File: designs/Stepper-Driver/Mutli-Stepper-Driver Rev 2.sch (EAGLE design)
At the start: 59 parts, among them IC1 PIC24FJ64GB002, J1 22-05-7048-04, J10 SON_OF_DARK_POWERSCH_22-05-70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, J11 SON_OF_DARK_POWERSCH_22-05-70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, J12 SON_OF_DARK_POWERSCH_22-05-70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, J2 22-05-7048-04, J3 22-05-7048-04, J4 22-05-7048-04, J5 22-05-7048-04, J6 22-05-7048-04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

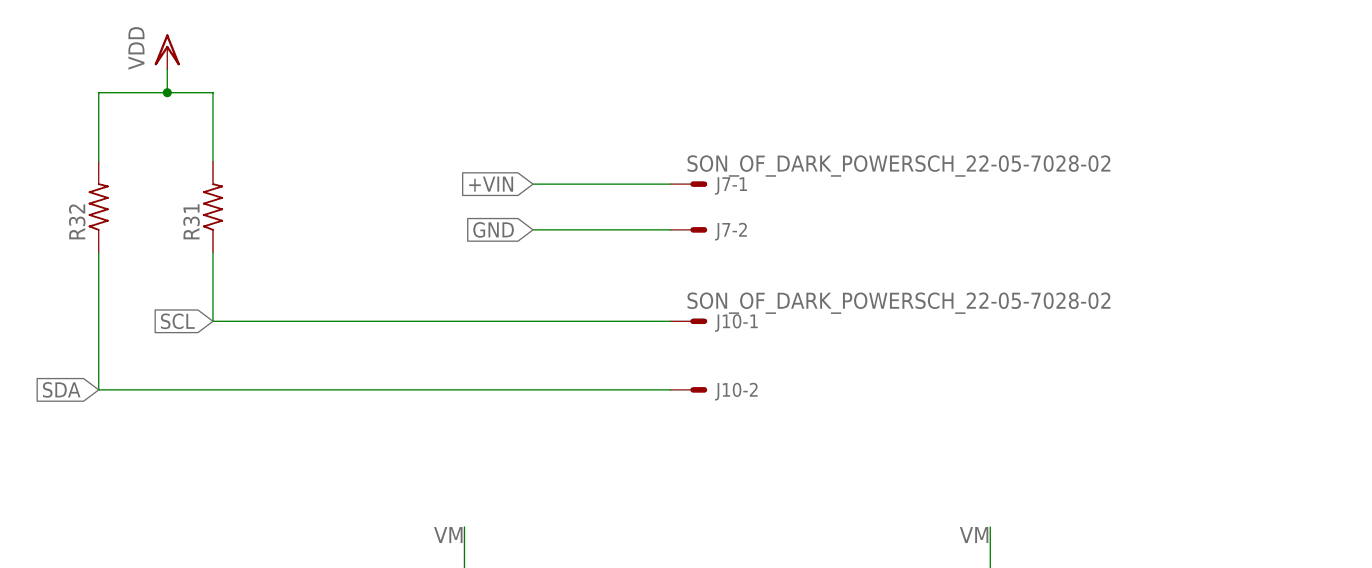
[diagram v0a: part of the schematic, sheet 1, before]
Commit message: removed extra part
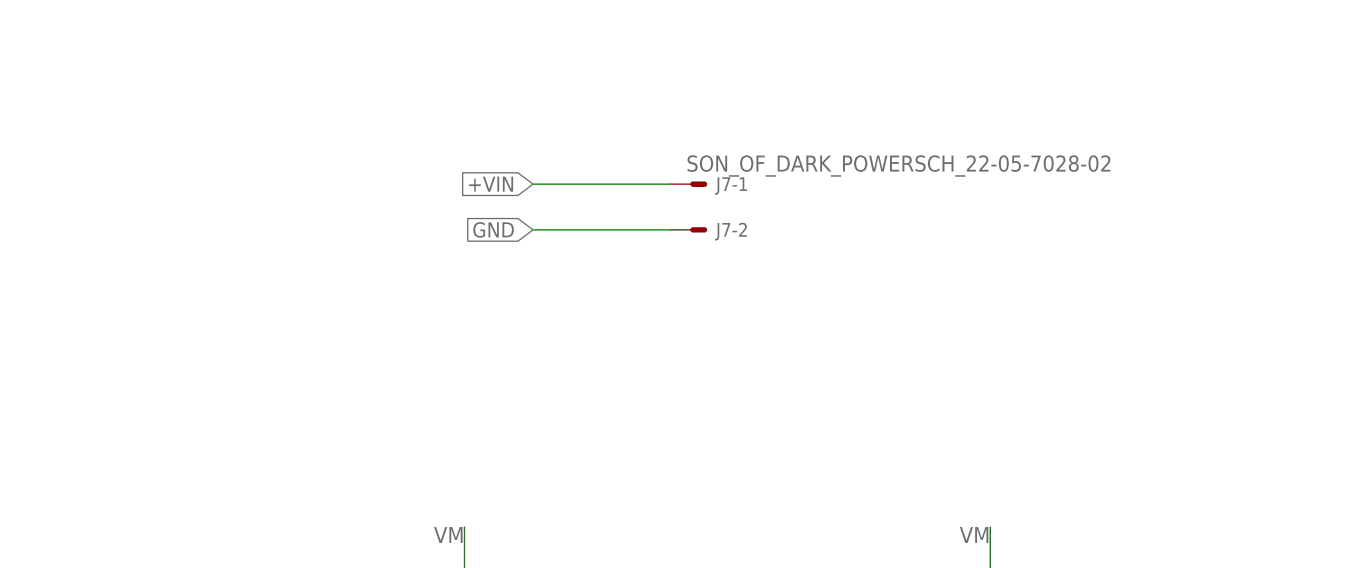
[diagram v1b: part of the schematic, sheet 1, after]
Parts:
- removed J10: SON_OF_DARK_POWERSCH_22-05-7028-02, MotherboardRev2:SON_OF_DARK_POWERSCH_22-05-7028-02
- removed R31, R32: (no value), rcl:R-US_R0805
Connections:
- removed net SCL: J10-1.S, R31.1
- removed net SDA: J10-2.S, R32.1
- net VDD: no longer R31.2, R32.2
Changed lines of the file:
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@@
 <part name="VDD6" library="supply1" deviceset="VDD" device=""/>
 <part name="GND29" library="supply1" deviceset="GND" device=""/>
-<part name="J10" library="MotherboardRev2" deviceset="SON_OF_DARK_POWERSCH_22-?-02" device="05-7028"/>
-<part name="R31" library="rcl" deviceset="R-US_" device="R0805"/>
-<part name="R32" library="rcl" deviceset="R-US_" device="R0805"/>
-<part name="VDD7" library="supply1" deviceset="VDD" device=""/>
 <part name="R33" library="rcl" deviceset="R-US_" device="R0805"/>
 <part name="LED1" library="led" deviceset="LED" device="CHIPLED_0805"/>
@@
 <instance part="VDD6" gate="G$1" x="119.38" y="76.2"/>
 <instance part="GND29" gate="1" x="129.54" y="22.86"/>
-<instance part="J10" gate="-1" x="81.28" y="218.44"/>
-<instance part="J10" gate="-2" x="81.28" y="210.82"/>
-<instance part="R31" gate="G$1" x="27.94" y="231.14" rot="R90"/>
-<instance part="R32" gate="G$1" x="15.24" y="231.14" rot="R90"/>
-<instance part="VDD7" gate="G$1" x="22.86" y="248.92"/>
 <instance part="R33" gate="G$1" x="170.18" y="157.48" rot="R90"/>
 <instance part="LED1" gate="G$1" x="170.18" y="147.32"/>
@@
 </segment>
 </net>
-<net name="SDA" class="0">
-<segment>
-<pinref part="J10" gate="-2" pin="S"/>
-<wire x1="78.74" y1="210.82" x2="15.24" y2="210.82" width="0.1524" layer="91"/>
-<pinref part="R32" gate="G$1" pin="1"/>
-<wire x1="15.24" y1="226.06" x2="15.24" y2="210.82" width="0.1524" layer="91"/>
-<label x="15.24" y="210.82" size="1.6764" layer="95" rot="R180" xref="yes"/>
-</segment>
-</net>
 <net name="PGD1" class="0">
 <segment>
@@
 <wire x1="101.6" y1="53.34" x2="91.44" y2="53.34" width="0.1524" layer="91"/>
 <label x="91.44" y="53.34" size="1.6764" layer="95" rot="R180" xref="yes"/>
-</segment>
-</net>
-<net name="SCL" class="0">
-<segment>
-<pinref part="J10" gate="-1" pin="S"/>
-<wire x1="78.74" y1="218.44" x2="27.94" y2="218.44" width="0.1524" layer="91"/>
-<pinref part="R31" gate="G$1" pin="1"/>
-<wire x1="27.94" y1="226.06" x2="27.94" y2="218.44" width="0.1524" layer="91"/>
-<label x="27.94" y="218.44" size="1.6764" layer="95" rot="R180" xref="yes"/>
 </segment>
 </net>
@@
 </segment>
 <segment>
-<pinref part="R32" gate="G$1" pin="2"/>
-<wire x1="15.24" y1="236.22" x2="15.24" y2="243.84" width="0.1524" layer="91"/>
-<pinref part="R31" gate="G$1" pin="2"/>
-<wire x1="15.24" y1="243.84" x2="22.86" y2="243.84" width="0.1524" layer="91"/>
-<wire x1="22.86" y1="243.84" x2="27.94" y2="243.84" width="0.1524" layer="91"/>
-<wire x1="27.94" y1="243.84" x2="27.94" y2="236.22" width="0.1524" layer="91"/>
-<wire x1="22.86" y1="243.84" x2="22.86" y2="246.38" width="0.1524" layer="91"/>
-<junction x="22.86" y="243.84"/>
-<pinref part="VDD7" gate="G$1" pin="VDD"/>
-</segment>
-<segment>
